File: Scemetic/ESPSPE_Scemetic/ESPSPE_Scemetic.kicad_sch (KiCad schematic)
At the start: 56 parts, among them J1 Screw_Terminal_01x02, J2 Conn_01x01_Pin, SW1 RESET, T1 749070010, U1 DEVKIT_V1_ESP32-WROOM-32, U2 ADIN1110, Y2 CFPX-180_830105863709

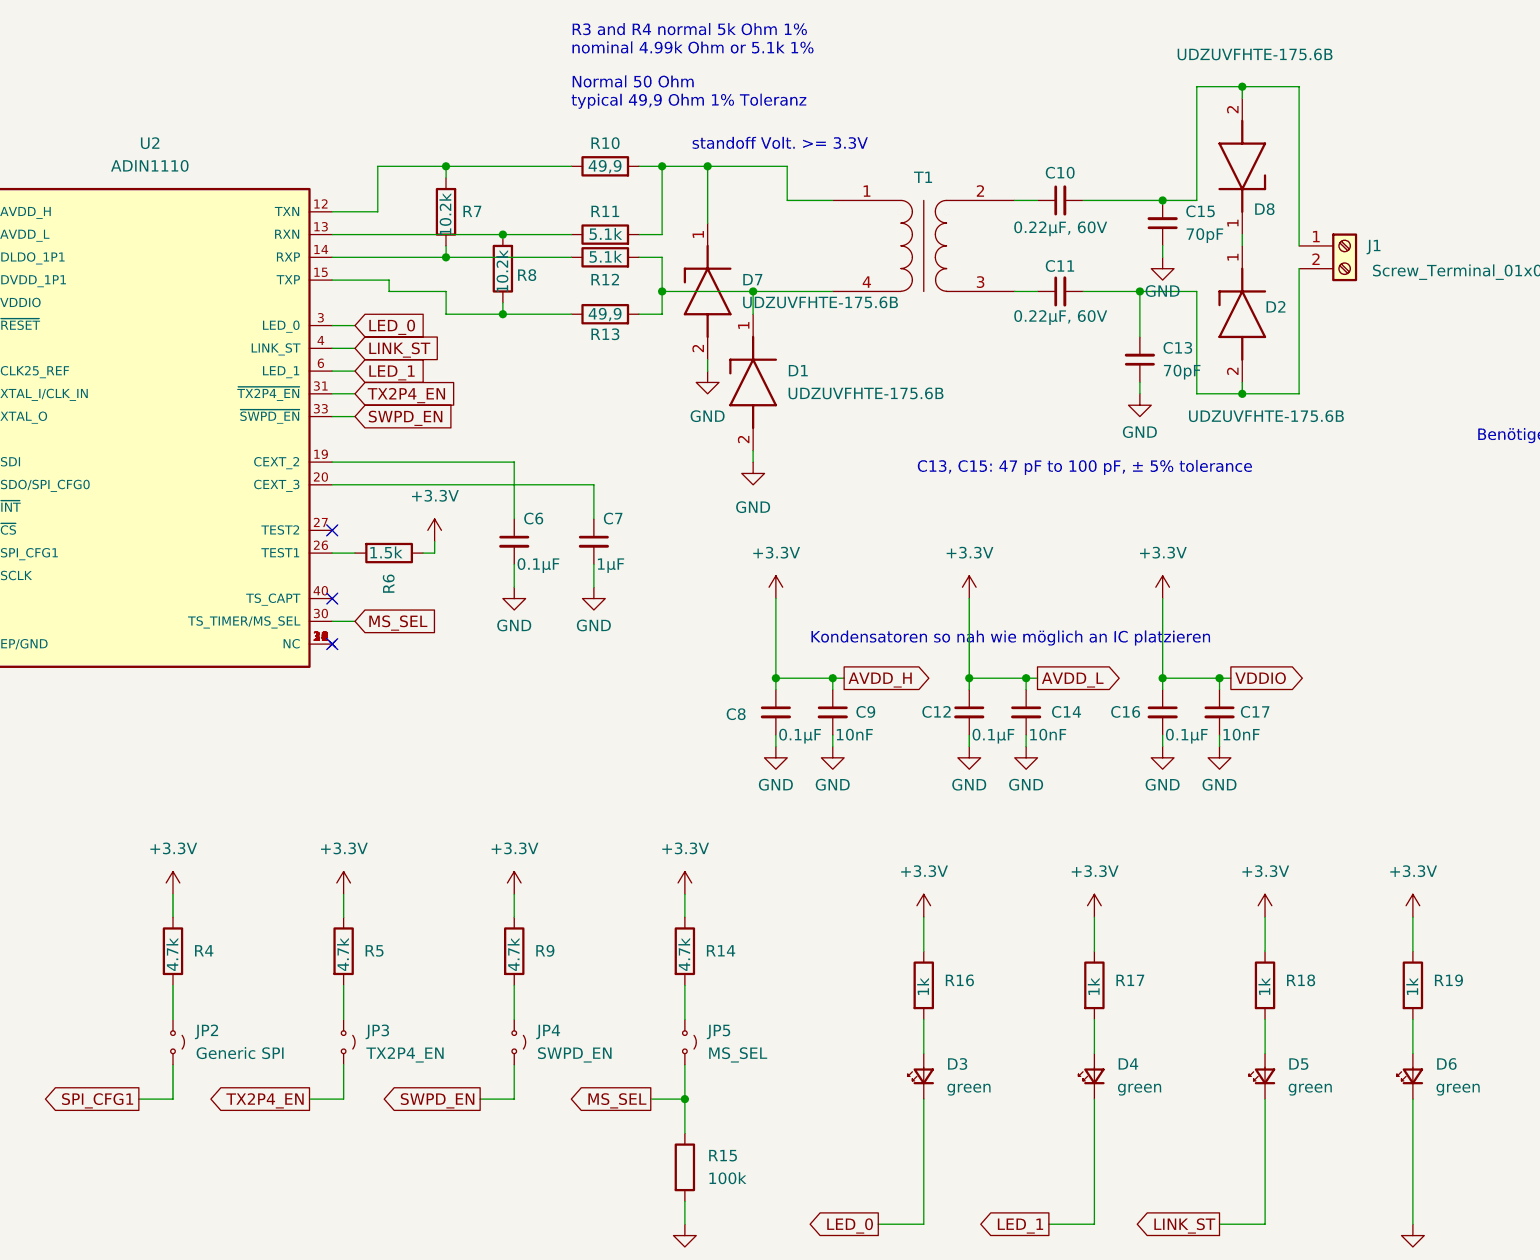
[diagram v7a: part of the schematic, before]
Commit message: Platine Bauteile kompakter angeordnet
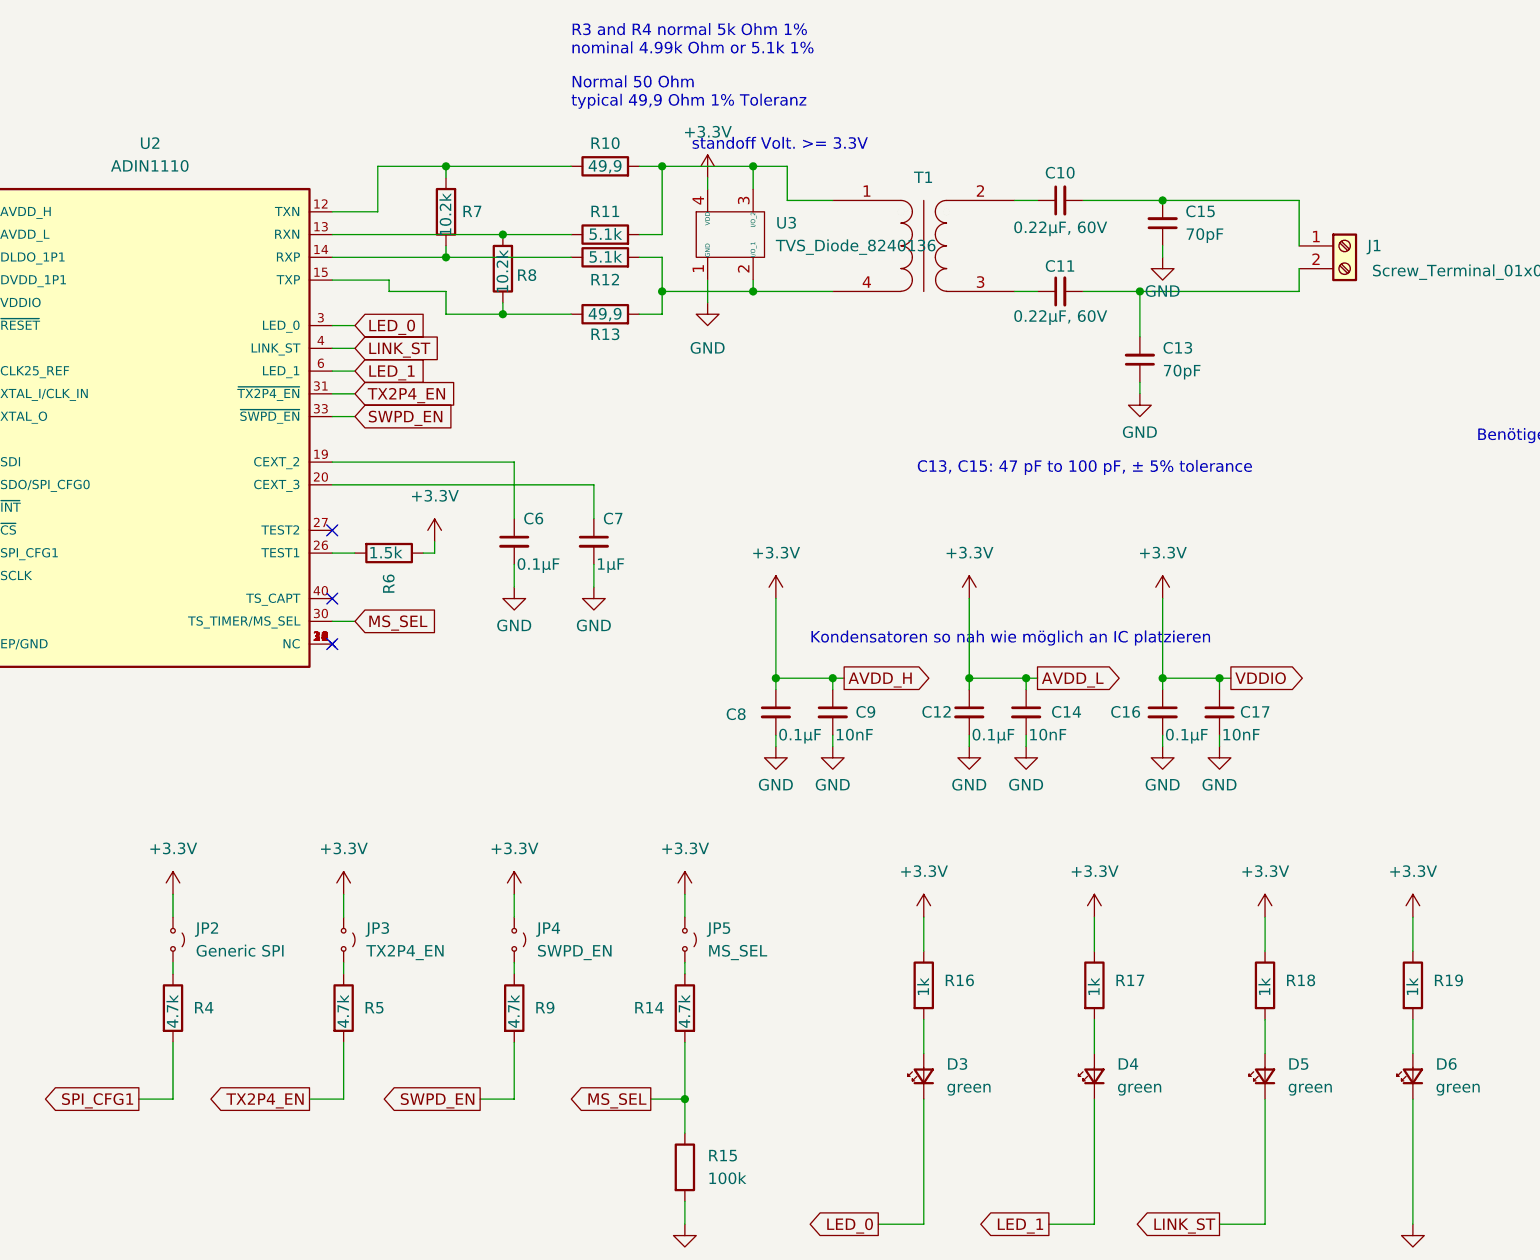
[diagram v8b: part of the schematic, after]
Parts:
- removed D1, D2, D7, D8: UDZUVFHTE-175.6B, KiCad_ZDiode_8pf:UDZUVFHTE1756B, symbol UDZUVFHTE-175_6B:UDZUVFHTE-175.6B
- added U3: TVS_Diode_8240136, TVS_Diode:TVS_Diode_8240136, symbol TVS_Diode:TVS_Diode_8240136
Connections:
- net +3.3V: now also JP2.1 (A), JP3.1 (A), JP4.1 (A), JP5.1 (A), U3.4 (VDD); no longer R14.1, R4.1, R5.1, R9.1
- net GND: now also U3.1 (GND)
- net MS_SEL: now also R14.2; no longer JP5.2 (B)
- net SPI_CFG1: now also R4.2; no longer JP2.2 (B)
- net SWPD_EN: now also R9.2; no longer JP4.2 (B)
- net TX2P4_EN: now also R5.2; no longer JP3.2 (B)
- net at R12.2, R13.2, T1.4: now also U3.2 (I/O_1)
- net at R10.2, R11.2, T1.1: now also U3.3 (I/O_2)
- new net: JP5.2 (B), R14.1
- new net: JP2.2 (B), R4.1
- new net: JP3.2 (B), R5.1
- new net: JP4.2 (B), R9.1
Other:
- moved on the sheet: JP2, JP3, JP4, JP5, R14, R4, R5, R9
